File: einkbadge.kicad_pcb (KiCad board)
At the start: 2 copper layers, 7.7 x 0.9 mm, 83 parts, among them J3 USB_C_Receptacle_USB2.0_14P, J4 Conn_01x03, J6 lipo, Q1 AO3401A, Q6 Si1308EDL, SW21 SW_Push, SW22 SW_Push, SW23 SW_Push, SW3 SW_Push, SW4 SW_Push, SW5 SW_SPDT, SW7 SW_Push, U11 SRV05-4, U18 ST25DV04K-JFR6D3, U5 RP2350_60QFN, U6 NCP1117-3.3_SOT223, U9 TP4056-42-ESOP8, Y1 ABM8-272-T3

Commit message: pcb routing almost done
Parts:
- removed C100, C101, C102, C103, C104, C95, C96, C97, C98, C99: 1uF, Capacitor_SMD:C_0402_1005Metric
- removed C105, C106: 4.7uF, Capacitor_SMD:C_0603_1608Metric
- removed C107: 0.1uF, Capacitor_SMD:C_0402_1005Metric
- removed C108: 33pF, Capacitor_SMD:C_0402_1005Metric
- removed D13: LED, LED_SMD:LED_0402_1005Metric
- removed D15, D21, D22, D23: MBR0530, Diode_SMD:D_SOD-123
- removed H5, H6, H7, H8: MountingHole, MountingHole:MountingHole_2.2mm_M2_Pad_Via
- removed J3: USB_C_Receptacle_USB2.0_14P, Connector_USB:USB_C_Receptacle_GCT_USB4105-xx-A_16P_TopMnt_Horizontal
- removed J4: Conn_01x03, Connector_PinHeader_1.00mm:PinHeader_1x03_P1.00mm_Vertical
- removed J6: lipo, Connector_JST:JST_PH_B2B-PH-K_1x02_P2.00mm_Vertical
- removed L6: 47uH 500mA, Inductor_SMD:L_APV_ANR4018
- removed Q6: Si1308EDL, Package_TO_SOT_SMD:SOT-323_SC-70
- removed R29: 2.2R, Resistor_SMD:R_0402_1005Metric
- removed R30: 1M, Resistor_SMD:R_0402_1005Metric
- removed R31: 47, Resistor_SMD:R_0402_1005Metric
- removed R32, R38, R45: 10k, Resistor_SMD:R_0402_1005Metric
- removed R33: 33, Resistor_SMD:R_0402_1005Metric
- removed R34, R35, R43: 5.1k, Resistor_SMD:R_0402_1005Metric
- removed R36, R37: 27, Resistor_SMD:R_0402_1005Metric
- removed R39, R44: 1.5k, Resistor_SMD:R_0402_1005Metric
- removed R40, R42: 1k, Resistor_SMD:R_0402_1005Metric
- removed R41: 1K, Resistor_SMD:R_0402_1005Metric
- removed SW21, SW22, SW23, SW7: SW_Push, Button_Switch_THT:SW_PUSH-12mm
- removed U11: SRV05-4, Package_TO_SOT_SMD:SOT-23-6
- removed U18: ST25DV04K-JFR6D3, Package_DFN_QFN:ST_UFDFPN-12-1EP_3x3mm_P0.5mm_EP1.4x2.55mm
- removed U6: NCP1117-3.3_SOT223, Package_TO_SOT_SMD:SOT-223-3_TabPin2
- removed U9: TP4056-42-ESOP8, Package_SO:SOIC-8-1EP_3.9x4.9mm_P1.27mm_EP2.41x3.3mm_ThermalVias
- added C18: 100n, Capacitor_SMD:C_0402_1005Metric, B.Cu at (198.1, 108.6)
- added C21: 4.7uF, Capacitor_SMD:C_0603_1608Metric, B.Cu at (169.2, 105.6)
- added C24: 1uF, Capacitor_SMD:C_0402_1005Metric, B.Cu at (162.3, 95.3)
- added C25: 1uF, Capacitor_SMD:C_0402_1005Metric, B.Cu at (162.3, 100.5)
- added C26: 1uF, Capacitor_SMD:C_0402_1005Metric, B.Cu at (162.3, 101.4)
- added C27: 1uF, Capacitor_SMD:C_0402_1005Metric, B.Cu at (162.3, 103.4)
- added C28: 1uF, Capacitor_SMD:C_0402_1005Metric, B.Cu at (162.3, 105.7)
- added C29: 1uF, Capacitor_SMD:C_0402_1005Metric, B.Cu at (162.3, 108.2)
- added C30: 1uF, Capacitor_SMD:C_0402_1005Metric, B.Cu at (162.3, 96.3)
- added C31: 1uF, Capacitor_SMD:C_0402_1005Metric, B.Cu at (162.3, 102.4)
- added C32: 1uF, Capacitor_SMD:C_0402_1005Metric, B.Cu at (162.3, 104.4)
- added C33: 1uF, Capacitor_SMD:C_0402_1005Metric, B.Cu at (162.3, 106.9)
- added D1: MBR0530, Diode_SMD:D_SOD-123, B.Cu at (165.9, 109.1)
- added D2: MBR0530, Diode_SMD:D_SOD-123, B.Cu at (165.9, 106.6)
- added D3: MBR0530, Diode_SMD:D_SOD-123, B.Cu at (165.9, 104.1)
- added D4: LED, LED_SMD:LED_0805_2012Metric, B.Cu at (232.4, 83.3)
- added H1: MountingHole, MountingHole:MountingHole_2.2mm_M2_Pad_Via, F.Cu at (156.1, 124.2)
- added H2: MountingHole, MountingHole:MountingHole_2.2mm_M2_Pad_Via, F.Cu at (252.6, 124.2)
- added H3: MountingHole, MountingHole:MountingHole_2.2mm_M2_Pad_Via, F.Cu at (156.1, 157.4)
- added H4: MountingHole, MountingHole:MountingHole_2.2mm_M2_Pad_Via, F.Cu at (252.6, 157.3)
- added J1: USB_C_Receptacle_USB2.0_14P, Connector_USB:USB_C_Receptacle_GCT_USB4105-xx-A_16P_TopMnt_Horizontal, B.Cu at (243.1, 159.4)
- added J2: Conn_01x03, Connector_PinHeader_2.54mm:PinHeader_1x03_P2.54mm_Vertical, B.Cu at (152.9, 117.0)
- added L2: 47uH 500mA, Inductor_SMD:L_APV_ANR4018, B.Cu at (166.5, 99.9)
- added L3: NFC antenna, ant:KiCadAntenna, F.Cu at (254.6, 82.0)
- added R1: 5.1k, Resistor_SMD:R_0402_1005Metric, B.Cu at (245.2, 153.5)
- added R10: 1M, Resistor_SMD:R_0402_1005Metric, B.Cu at (166.3, 92.9)
- added R11: 10k, Resistor_SMD:R_0402_1005Metric, B.Cu at (236.4, 93.9)
- added R12: 2.2R, Resistor_SMD:R_0402_1005Metric, B.Cu at (166.3, 94.0)
- added R13: 47, Resistor_SMD:R_0402_1005Metric, B.Cu at (234.8, 83.3)
- added R14: 10k, Resistor_SMD:R_0402_1005Metric, B.Cu at (232.9, 92.8)
- added R2: 5.1k, Resistor_SMD:R_0402_1005Metric, B.Cu at (240.6, 153.5)
- added R3: 33, Resistor_SMD:R_0402_1005Metric, B.Cu at (209.4, 103.1)
- added R4: 1k, Resistor_SMD:R_0402_1005Metric, B.Cu at (223.1, 112.4)
- added R5: 1k, Resistor_SMD:R_0402_1005Metric, B.Cu at (223.1, 102.0)
- added R6: 1K, Resistor_SMD:R_0402_1005Metric, B.Cu at (191.3, 91.9)
- added R7: 27, Resistor_SMD:R_0402_1005Metric, B.Cu at (204.1, 108.0)
- added R8: 27, Resistor_SMD:R_0402_1005Metric, B.Cu at (204.9, 107.2)
- added R9: 10k, Resistor_SMD:R_0402_1005Metric, B.Cu at (235.4, 93.9)
- added REF**10: TestPoint_THTPad_D2.0mm_Drill1.0mm, TestPoint:TestPoint_THTPad_D2.0mm_Drill1.0mm, F.Cu at (175.1, 122.9)
- added REF**100: TestPoint_THTPad_D2.0mm_Drill1.0mm, TestPoint:TestPoint_THTPad_D2.0mm_Drill1.0mm, F.Cu at (200.5, 128.0)
- added REF**101: TestPoint_THTPad_D2.0mm_Drill1.0mm, TestPoint:TestPoint_THTPad_D2.0mm_Drill1.0mm, F.Cu at (203.1, 128.0)
- added REF**102: TestPoint_THTPad_D2.0mm_Drill1.0mm, TestPoint:TestPoint_THTPad_D2.0mm_Drill1.0mm, F.Cu at (205.6, 128.0)
- added REF**103: TestPoint_THTPad_D2.0mm_Drill1.0mm, TestPoint:TestPoint_THTPad_D2.0mm_Drill1.0mm, F.Cu at (208.1, 128.0)
- added REF**104: TestPoint_THTPad_D2.0mm_Drill1.0mm, TestPoint:TestPoint_THTPad_D2.0mm_Drill1.0mm, F.Cu at (210.7, 128.0)
- added REF**105: TestPoint_THTPad_D2.0mm_Drill1.0mm, TestPoint:TestPoint_THTPad_D2.0mm_Drill1.0mm, F.Cu at (213.2, 128.0)
- added REF**106: TestPoint_THTPad_D2.0mm_Drill1.0mm, TestPoint:TestPoint_THTPad_D2.0mm_Drill1.0mm, F.Cu at (215.8, 128.0)
- added REF**107: TestPoint_THTPad_D2.0mm_Drill1.0mm, TestPoint:TestPoint_THTPad_D2.0mm_Drill1.0mm, F.Cu at (218.3, 128.0)
- added REF**108: TestPoint_THTPad_D2.0mm_Drill1.0mm, TestPoint:TestPoint_THTPad_D2.0mm_Drill1.0mm, F.Cu at (220.8, 128.0)
- added REF**109: TestPoint_THTPad_D2.0mm_Drill1.0mm, TestPoint:TestPoint_THTPad_D2.0mm_Drill1.0mm, F.Cu at (223.4, 128.0)
- added REF**11: TestPoint_THTPad_D2.0mm_Drill1.0mm, TestPoint:TestPoint_THTPad_D2.0mm_Drill1.0mm, F.Cu at (177.7, 122.9)
- added REF**110: TestPoint_THTPad_D2.0mm_Drill1.0mm, TestPoint:TestPoint_THTPad_D2.0mm_Drill1.0mm, F.Cu at (225.9, 128.0)
- added REF**111: TestPoint_THTPad_D2.0mm_Drill1.0mm, TestPoint:TestPoint_THTPad_D2.0mm_Drill1.0mm, F.Cu at (228.5, 128.0)
- added REF**112: TestPoint_THTPad_D2.0mm_Drill1.0mm, TestPoint:TestPoint_THTPad_D2.0mm_Drill1.0mm, F.Cu at (231.0, 128.0)
- added REF**113: TestPoint_THTPad_D2.0mm_Drill1.0mm, TestPoint:TestPoint_THTPad_D2.0mm_Drill1.0mm, F.Cu at (233.5, 128.0)
- added REF**12: TestPoint_THTPad_D2.0mm_Drill1.0mm, TestPoint:TestPoint_THTPad_D2.0mm_Drill1.0mm, F.Cu at (180.2, 122.9)
- added REF**122: TestPoint_THTPad_D2.0mm_Drill1.0mm, TestPoint:TestPoint_THTPad_D2.0mm_Drill1.0mm, F.Cu at (154.8, 130.6)
- added REF**123: TestPoint_THTPad_D2.0mm_Drill1.0mm, TestPoint:TestPoint_THTPad_D2.0mm_Drill1.0mm, F.Cu at (157.3, 130.6)
- added REF**124: TestPoint_THTPad_D2.0mm_Drill1.0mm, TestPoint:TestPoint_THTPad_D2.0mm_Drill1.0mm, F.Cu at (159.9, 130.6)
- added REF**125: TestPoint_THTPad_D2.0mm_Drill1.0mm, TestPoint:TestPoint_THTPad_D2.0mm_Drill1.0mm, F.Cu at (162.4, 130.6)
- added REF**126: TestPoint_THTPad_D2.0mm_Drill1.0mm, TestPoint:TestPoint_THTPad_D2.0mm_Drill1.0mm, F.Cu at (165.0, 130.6)
- added REF**127: TestPoint_THTPad_D2.0mm_Drill1.0mm, TestPoint:TestPoint_THTPad_D2.0mm_Drill1.0mm, F.Cu at (167.5, 130.6)
- added REF**128: TestPoint_THTPad_D2.0mm_Drill1.0mm, TestPoint:TestPoint_THTPad_D2.0mm_Drill1.0mm, F.Cu at (170.0, 130.6)
- added REF**13: TestPoint_THTPad_D2.0mm_Drill1.0mm, TestPoint:TestPoint_THTPad_D2.0mm_Drill1.0mm, F.Cu at (182.7, 122.9)
- added REF**135: TestPoint_THTPad_D2.0mm_Drill1.0mm, TestPoint:TestPoint_THTPad_D2.0mm_Drill1.0mm, F.Cu at (187.8, 130.6)
- added REF**136: TestPoint_THTPad_D2.0mm_Drill1.0mm, TestPoint:TestPoint_THTPad_D2.0mm_Drill1.0mm, F.Cu at (190.4, 130.6)
- added REF**137: TestPoint_THTPad_D2.0mm_Drill1.0mm, TestPoint:TestPoint_THTPad_D2.0mm_Drill1.0mm, F.Cu at (192.9, 130.6)
- added REF**138: TestPoint_THTPad_D2.0mm_Drill1.0mm, TestPoint:TestPoint_THTPad_D2.0mm_Drill1.0mm, F.Cu at (195.4, 130.6)
- added REF**139: TestPoint_THTPad_D2.0mm_Drill1.0mm, TestPoint:TestPoint_THTPad_D2.0mm_Drill1.0mm, F.Cu at (198.0, 130.6)
- added REF**14: TestPoint_THTPad_D2.0mm_Drill1.0mm, TestPoint:TestPoint_THTPad_D2.0mm_Drill1.0mm, F.Cu at (185.3, 122.9)
- added REF**140: TestPoint_THTPad_D2.0mm_Drill1.0mm, TestPoint:TestPoint_THTPad_D2.0mm_Drill1.0mm, F.Cu at (200.5, 130.6)
- added REF**141: TestPoint_THTPad_D2.0mm_Drill1.0mm, TestPoint:TestPoint_THTPad_D2.0mm_Drill1.0mm, F.Cu at (203.1, 130.6)
- added REF**142: TestPoint_THTPad_D2.0mm_Drill1.0mm, TestPoint:TestPoint_THTPad_D2.0mm_Drill1.0mm, F.Cu at (205.6, 130.6)
- added REF**143: TestPoint_THTPad_D2.0mm_Drill1.0mm, TestPoint:TestPoint_THTPad_D2.0mm_Drill1.0mm, F.Cu at (208.1, 130.6)
- added REF**144: TestPoint_THTPad_D2.0mm_Drill1.0mm, TestPoint:TestPoint_THTPad_D2.0mm_Drill1.0mm, F.Cu at (210.7, 130.6)
- added REF**145: TestPoint_THTPad_D2.0mm_Drill1.0mm, TestPoint:TestPoint_THTPad_D2.0mm_Drill1.0mm, F.Cu at (213.2, 130.6)
- added REF**146: TestPoint_THTPad_D2.0mm_Drill1.0mm, TestPoint:TestPoint_THTPad_D2.0mm_Drill1.0mm, F.Cu at (215.8, 130.6)
- added REF**147: TestPoint_THTPad_D2.0mm_Drill1.0mm, TestPoint:TestPoint_THTPad_D2.0mm_Drill1.0mm, F.Cu at (218.3, 130.6)
- added REF**148: TestPoint_THTPad_D2.0mm_Drill1.0mm, TestPoint:TestPoint_THTPad_D2.0mm_Drill1.0mm, F.Cu at (220.8, 130.6)
- added REF**149: TestPoint_THTPad_D2.0mm_Drill1.0mm, TestPoint:TestPoint_THTPad_D2.0mm_Drill1.0mm, F.Cu at (223.4, 130.6)
- added REF**15: TestPoint_THTPad_D2.0mm_Drill1.0mm, TestPoint:TestPoint_THTPad_D2.0mm_Drill1.0mm, F.Cu at (187.8, 122.9)
- added REF**150: TestPoint_THTPad_D2.0mm_Drill1.0mm, TestPoint:TestPoint_THTPad_D2.0mm_Drill1.0mm, F.Cu at (225.9, 130.6)
- added REF**151: TestPoint_THTPad_D2.0mm_Drill1.0mm, TestPoint:TestPoint_THTPad_D2.0mm_Drill1.0mm, F.Cu at (228.5, 130.6)
- added REF**152: TestPoint_THTPad_D2.0mm_Drill1.0mm, TestPoint:TestPoint_THTPad_D2.0mm_Drill1.0mm, F.Cu at (231.0, 130.6)
- added REF**153: TestPoint_THTPad_D2.0mm_Drill1.0mm, TestPoint:TestPoint_THTPad_D2.0mm_Drill1.0mm, F.Cu at (233.5, 130.6)
- added REF**16: TestPoint_THTPad_D2.0mm_Drill1.0mm, TestPoint:TestPoint_THTPad_D2.0mm_Drill1.0mm, F.Cu at (190.4, 122.9)
- added REF**162: TestPoint_THTPad_D2.0mm_Drill1.0mm, TestPoint:TestPoint_THTPad_D2.0mm_Drill1.0mm, F.Cu at (154.8, 133.1)
- added REF**163: TestPoint_THTPad_D2.0mm_Drill1.0mm, TestPoint:TestPoint_THTPad_D2.0mm_Drill1.0mm, F.Cu at (157.3, 133.1)
- added REF**164: TestPoint_THTPad_D2.0mm_Drill1.0mm, TestPoint:TestPoint_THTPad_D2.0mm_Drill1.0mm, F.Cu at (159.9, 133.1)
- added REF**165: TestPoint_THTPad_D2.0mm_Drill1.0mm, TestPoint:TestPoint_THTPad_D2.0mm_Drill1.0mm, F.Cu at (162.4, 133.1)
- added REF**166: TestPoint_THTPad_D2.0mm_Drill1.0mm, TestPoint:TestPoint_THTPad_D2.0mm_Drill1.0mm, F.Cu at (165.0, 133.1)
- added REF**167: TestPoint_THTPad_D2.0mm_Drill1.0mm, TestPoint:TestPoint_THTPad_D2.0mm_Drill1.0mm, F.Cu at (167.5, 133.1)
- added REF**168: TestPoint_THTPad_D2.0mm_Drill1.0mm, TestPoint:TestPoint_THTPad_D2.0mm_Drill1.0mm, F.Cu at (170.0, 133.1)
- added REF**169: TestPoint_THTPad_D2.0mm_Drill1.0mm, TestPoint:TestPoint_THTPad_D2.0mm_Drill1.0mm, F.Cu at (172.6, 133.1)
- added REF**17: TestPoint_THTPad_D2.0mm_Drill1.0mm, TestPoint:TestPoint_THTPad_D2.0mm_Drill1.0mm, F.Cu at (192.9, 122.9)
- added REF**170: TestPoint_THTPad_D2.0mm_Drill1.0mm, TestPoint:TestPoint_THTPad_D2.0mm_Drill1.0mm, F.Cu at (175.1, 133.1)
- added REF**171: TestPoint_THTPad_D2.0mm_Drill1.0mm, TestPoint:TestPoint_THTPad_D2.0mm_Drill1.0mm, F.Cu at (177.7, 133.1)
- added REF**172: TestPoint_THTPad_D2.0mm_Drill1.0mm, TestPoint:TestPoint_THTPad_D2.0mm_Drill1.0mm, F.Cu at (180.2, 133.1)
- added REF**173: TestPoint_THTPad_D2.0mm_Drill1.0mm, TestPoint:TestPoint_THTPad_D2.0mm_Drill1.0mm, F.Cu at (182.7, 133.1)
- added REF**174: TestPoint_THTPad_D2.0mm_Drill1.0mm, TestPoint:TestPoint_THTPad_D2.0mm_Drill1.0mm, F.Cu at (185.3, 133.1)
- added REF**175: TestPoint_THTPad_D2.0mm_Drill1.0mm, TestPoint:TestPoint_THTPad_D2.0mm_Drill1.0mm, F.Cu at (187.8, 133.1)
- added REF**176: TestPoint_THTPad_D2.0mm_Drill1.0mm, TestPoint:TestPoint_THTPad_D2.0mm_Drill1.0mm, F.Cu at (190.4, 133.1)
- added REF**177: TestPoint_THTPad_D2.0mm_Drill1.0mm, TestPoint:TestPoint_THTPad_D2.0mm_Drill1.0mm, F.Cu at (192.9, 133.1)
- added REF**178: TestPoint_THTPad_D2.0mm_Drill1.0mm, TestPoint:TestPoint_THTPad_D2.0mm_Drill1.0mm, F.Cu at (195.4, 133.1)
- added REF**179: TestPoint_THTPad_D2.0mm_Drill1.0mm, TestPoint:TestPoint_THTPad_D2.0mm_Drill1.0mm, F.Cu at (198.0, 133.1)
- added REF**18: TestPoint_THTPad_D2.0mm_Drill1.0mm, TestPoint:TestPoint_THTPad_D2.0mm_Drill1.0mm, F.Cu at (195.4, 122.9)
- added REF**180: TestPoint_THTPad_D2.0mm_Drill1.0mm, TestPoint:TestPoint_THTPad_D2.0mm_Drill1.0mm, F.Cu at (200.5, 133.1)
- added REF**181: TestPoint_THTPad_D2.0mm_Drill1.0mm, TestPoint:TestPoint_THTPad_D2.0mm_Drill1.0mm, F.Cu at (203.1, 133.1)
- added REF**182: TestPoint_THTPad_D2.0mm_Drill1.0mm, TestPoint:TestPoint_THTPad_D2.0mm_Drill1.0mm, F.Cu at (205.6, 133.1)
- added REF**183: TestPoint_THTPad_D2.0mm_Drill1.0mm, TestPoint:TestPoint_THTPad_D2.0mm_Drill1.0mm, F.Cu at (208.1, 133.1)
- added REF**184: TestPoint_THTPad_D2.0mm_Drill1.0mm, TestPoint:TestPoint_THTPad_D2.0mm_Drill1.0mm, F.Cu at (210.7, 133.1)
- added REF**185: TestPoint_THTPad_D2.0mm_Drill1.0mm, TestPoint:TestPoint_THTPad_D2.0mm_Drill1.0mm, F.Cu at (213.2, 133.1)
- added REF**186: TestPoint_THTPad_D2.0mm_Drill1.0mm, TestPoint:TestPoint_THTPad_D2.0mm_Drill1.0mm, F.Cu at (215.8, 133.1)
- added REF**187: TestPoint_THTPad_D2.0mm_Drill1.0mm, TestPoint:TestPoint_THTPad_D2.0mm_Drill1.0mm, F.Cu at (218.3, 133.1)
- added REF**188: TestPoint_THTPad_D2.0mm_Drill1.0mm, TestPoint:TestPoint_THTPad_D2.0mm_Drill1.0mm, F.Cu at (220.8, 133.1)
- added REF**189: TestPoint_THTPad_D2.0mm_Drill1.0mm, TestPoint:TestPoint_THTPad_D2.0mm_Drill1.0mm, F.Cu at (223.4, 133.1)
- added REF**19: TestPoint_THTPad_D2.0mm_Drill1.0mm, TestPoint:TestPoint_THTPad_D2.0mm_Drill1.0mm, F.Cu at (198.0, 122.9)
- added REF**190: TestPoint_THTPad_D2.0mm_Drill1.0mm, TestPoint:TestPoint_THTPad_D2.0mm_Drill1.0mm, F.Cu at (225.9, 133.1)
- added REF**191: TestPoint_THTPad_D2.0mm_Drill1.0mm, TestPoint:TestPoint_THTPad_D2.0mm_Drill1.0mm, F.Cu at (228.5, 133.1)
- added REF**192: TestPoint_THTPad_D2.0mm_Drill1.0mm, TestPoint:TestPoint_THTPad_D2.0mm_Drill1.0mm, F.Cu at (231.0, 133.1)
- added REF**193: TestPoint_THTPad_D2.0mm_Drill1.0mm, TestPoint:TestPoint_THTPad_D2.0mm_Drill1.0mm, F.Cu at (233.5, 133.1)
- added REF**194: TestPoint_THTPad_D2.0mm_Drill1.0mm, TestPoint:TestPoint_THTPad_D2.0mm_Drill1.0mm, F.Cu at (236.1, 133.1)
- added REF**20: TestPoint_THTPad_D2.0mm_Drill1.0mm, TestPoint:TestPoint_THTPad_D2.0mm_Drill1.0mm, F.Cu at (200.5, 122.9)
- added REF**202: TestPoint_THTPad_D2.0mm_Drill1.0mm, TestPoint:TestPoint_THTPad_D2.0mm_Drill1.0mm, F.Cu at (154.8, 135.6)
- added REF**203: TestPoint_THTPad_D2.0mm_Drill1.0mm, TestPoint:TestPoint_THTPad_D2.0mm_Drill1.0mm, F.Cu at (157.3, 135.6)
- added REF**204: TestPoint_THTPad_D2.0mm_Drill1.0mm, TestPoint:TestPoint_THTPad_D2.0mm_Drill1.0mm, F.Cu at (159.9, 135.6)
- added REF**205: TestPoint_THTPad_D2.0mm_Drill1.0mm, TestPoint:TestPoint_THTPad_D2.0mm_Drill1.0mm, F.Cu at (162.4, 135.6)
- added REF**206: TestPoint_THTPad_D2.0mm_Drill1.0mm, TestPoint:TestPoint_THTPad_D2.0mm_Drill1.0mm, F.Cu at (165.0, 135.6)
- added REF**207: TestPoint_THTPad_D2.0mm_Drill1.0mm, TestPoint:TestPoint_THTPad_D2.0mm_Drill1.0mm, F.Cu at (167.5, 135.6)
- added REF**208: TestPoint_THTPad_D2.0mm_Drill1.0mm, TestPoint:TestPoint_THTPad_D2.0mm_Drill1.0mm, F.Cu at (170.0, 135.6)
- added REF**209: TestPoint_THTPad_D2.0mm_Drill1.0mm, TestPoint:TestPoint_THTPad_D2.0mm_Drill1.0mm, F.Cu at (172.6, 135.6)
- added REF**21: TestPoint_THTPad_D2.0mm_Drill1.0mm, TestPoint:TestPoint_THTPad_D2.0mm_Drill1.0mm, F.Cu at (203.1, 122.9)
- added REF**210: TestPoint_THTPad_D2.0mm_Drill1.0mm, TestPoint:TestPoint_THTPad_D2.0mm_Drill1.0mm, F.Cu at (175.1, 135.6)
- added REF**211: TestPoint_THTPad_D2.0mm_Drill1.0mm, TestPoint:TestPoint_THTPad_D2.0mm_Drill1.0mm, F.Cu at (177.7, 135.6)
- added REF**212: TestPoint_THTPad_D2.0mm_Drill1.0mm, TestPoint:TestPoint_THTPad_D2.0mm_Drill1.0mm, F.Cu at (180.2, 135.6)
- added REF**213: TestPoint_THTPad_D2.0mm_Drill1.0mm, TestPoint:TestPoint_THTPad_D2.0mm_Drill1.0mm, F.Cu at (182.7, 135.6)
- added REF**214: TestPoint_THTPad_D2.0mm_Drill1.0mm, TestPoint:TestPoint_THTPad_D2.0mm_Drill1.0mm, F.Cu at (185.3, 135.6)
- added REF**215: TestPoint_THTPad_D2.0mm_Drill1.0mm, TestPoint:TestPoint_THTPad_D2.0mm_Drill1.0mm, F.Cu at (187.8, 135.6)
- added REF**216: TestPoint_THTPad_D2.0mm_Drill1.0mm, TestPoint:TestPoint_THTPad_D2.0mm_Drill1.0mm, F.Cu at (190.4, 135.6)
- added REF**217: TestPoint_THTPad_D2.0mm_Drill1.0mm, TestPoint:TestPoint_THTPad_D2.0mm_Drill1.0mm, F.Cu at (192.9, 135.6)
- added REF**218: TestPoint_THTPad_D2.0mm_Drill1.0mm, TestPoint:TestPoint_THTPad_D2.0mm_Drill1.0mm, F.Cu at (195.4, 135.6)
- added REF**219: TestPoint_THTPad_D2.0mm_Drill1.0mm, TestPoint:TestPoint_THTPad_D2.0mm_Drill1.0mm, F.Cu at (198.0, 135.6)
- added REF**22: TestPoint_THTPad_D2.0mm_Drill1.0mm, TestPoint:TestPoint_THTPad_D2.0mm_Drill1.0mm, F.Cu at (205.6, 122.9)
- added REF**220: TestPoint_THTPad_D2.0mm_Drill1.0mm, TestPoint:TestPoint_THTPad_D2.0mm_Drill1.0mm, F.Cu at (200.5, 135.6)
- added REF**221: TestPoint_THTPad_D2.0mm_Drill1.0mm, TestPoint:TestPoint_THTPad_D2.0mm_Drill1.0mm, F.Cu at (203.1, 135.6)
- added REF**222: TestPoint_THTPad_D2.0mm_Drill1.0mm, TestPoint:TestPoint_THTPad_D2.0mm_Drill1.0mm, F.Cu at (205.6, 135.6)
- added REF**223: TestPoint_THTPad_D2.0mm_Drill1.0mm, TestPoint:TestPoint_THTPad_D2.0mm_Drill1.0mm, F.Cu at (208.1, 135.6)
- added REF**224: TestPoint_THTPad_D2.0mm_Drill1.0mm, TestPoint:TestPoint_THTPad_D2.0mm_Drill1.0mm, F.Cu at (210.7, 135.6)
- added REF**225: TestPoint_THTPad_D2.0mm_Drill1.0mm, TestPoint:TestPoint_THTPad_D2.0mm_Drill1.0mm, F.Cu at (213.2, 135.6)
- added REF**226: TestPoint_THTPad_D2.0mm_Drill1.0mm, TestPoint:TestPoint_THTPad_D2.0mm_Drill1.0mm, F.Cu at (215.8, 135.6)
- added REF**227: TestPoint_THTPad_D2.0mm_Drill1.0mm, TestPoint:TestPoint_THTPad_D2.0mm_Drill1.0mm, F.Cu at (218.3, 135.6)
- added REF**228: TestPoint_THTPad_D2.0mm_Drill1.0mm, TestPoint:TestPoint_THTPad_D2.0mm_Drill1.0mm, F.Cu at (220.8, 135.6)
- added REF**229: TestPoint_THTPad_D2.0mm_Drill1.0mm, TestPoint:TestPoint_THTPad_D2.0mm_Drill1.0mm, F.Cu at (223.4, 135.6)
- added REF**23: TestPoint_THTPad_D2.0mm_Drill1.0mm, TestPoint:TestPoint_THTPad_D2.0mm_Drill1.0mm, F.Cu at (208.1, 122.9)
- added REF**230: TestPoint_THTPad_D2.0mm_Drill1.0mm, TestPoint:TestPoint_THTPad_D2.0mm_Drill1.0mm, F.Cu at (225.9, 135.6)
- added REF**231: TestPoint_THTPad_D2.0mm_Drill1.0mm, TestPoint:TestPoint_THTPad_D2.0mm_Drill1.0mm, F.Cu at (228.5, 135.6)
- added REF**232: TestPoint_THTPad_D2.0mm_Drill1.0mm, TestPoint:TestPoint_THTPad_D2.0mm_Drill1.0mm, F.Cu at (231.0, 135.6)
- added REF**233: TestPoint_THTPad_D2.0mm_Drill1.0mm, TestPoint:TestPoint_THTPad_D2.0mm_Drill1.0mm, F.Cu at (233.5, 135.6)
- added REF**24: TestPoint_THTPad_D2.0mm_Drill1.0mm, TestPoint:TestPoint_THTPad_D2.0mm_Drill1.0mm, F.Cu at (210.7, 122.9)
- added REF**242: TestPoint_THTPad_D2.0mm_Drill1.0mm, TestPoint:TestPoint_THTPad_D2.0mm_Drill1.0mm, F.Cu at (154.8, 138.2)
- added REF**243: TestPoint_THTPad_D2.0mm_Drill1.0mm, TestPoint:TestPoint_THTPad_D2.0mm_Drill1.0mm, F.Cu at (157.3, 138.2)
- added REF**25: TestPoint_THTPad_D2.0mm_Drill1.0mm, TestPoint:TestPoint_THTPad_D2.0mm_Drill1.0mm, F.Cu at (213.2, 122.9)
- added REF**250: TestPoint_THTPad_D2.0mm_Drill1.0mm, TestPoint:TestPoint_THTPad_D2.0mm_Drill1.0mm, F.Cu at (175.1, 138.2)
- added REF**251: TestPoint_THTPad_D2.0mm_Drill1.0mm, TestPoint:TestPoint_THTPad_D2.0mm_Drill1.0mm, F.Cu at (177.7, 138.2)
- added REF**252: TestPoint_THTPad_D2.0mm_Drill1.0mm, TestPoint:TestPoint_THTPad_D2.0mm_Drill1.0mm, F.Cu at (180.2, 138.2)
- added REF**253: TestPoint_THTPad_D2.0mm_Drill1.0mm, TestPoint:TestPoint_THTPad_D2.0mm_Drill1.0mm, F.Cu at (182.7, 138.2)
- added REF**26: TestPoint_THTPad_D2.0mm_Drill1.0mm, TestPoint:TestPoint_THTPad_D2.0mm_Drill1.0mm, F.Cu at (215.8, 122.9)
- added REF**260: TestPoint_THTPad_D2.0mm_Drill1.0mm, TestPoint:TestPoint_THTPad_D2.0mm_Drill1.0mm, F.Cu at (200.5, 138.2)
- added REF**261: TestPoint_THTPad_D2.0mm_Drill1.0mm, TestPoint:TestPoint_THTPad_D2.0mm_Drill1.0mm, F.Cu at (203.1, 138.2)
- added REF**262: TestPoint_THTPad_D2.0mm_Drill1.0mm, TestPoint:TestPoint_THTPad_D2.0mm_Drill1.0mm, F.Cu at (205.6, 138.2)
- added REF**263: TestPoint_THTPad_D2.0mm_Drill1.0mm, TestPoint:TestPoint_THTPad_D2.0mm_Drill1.0mm, F.Cu at (208.1, 138.2)
- added REF**264: TestPoint_THTPad_D2.0mm_Drill1.0mm, TestPoint:TestPoint_THTPad_D2.0mm_Drill1.0mm, F.Cu at (210.7, 138.2)
- added REF**265: TestPoint_THTPad_D2.0mm_Drill1.0mm, TestPoint:TestPoint_THTPad_D2.0mm_Drill1.0mm, F.Cu at (213.2, 138.2)
- added REF**266: TestPoint_THTPad_D2.0mm_Drill1.0mm, TestPoint:TestPoint_THTPad_D2.0mm_Drill1.0mm, F.Cu at (215.8, 138.2)
- added REF**267: TestPoint_THTPad_D2.0mm_Drill1.0mm, TestPoint:TestPoint_THTPad_D2.0mm_Drill1.0mm, F.Cu at (218.3, 138.2)
- added REF**268: TestPoint_THTPad_D2.0mm_Drill1.0mm, TestPoint:TestPoint_THTPad_D2.0mm_Drill1.0mm, F.Cu at (220.8, 138.2)
- added REF**269: TestPoint_THTPad_D2.0mm_Drill1.0mm, TestPoint:TestPoint_THTPad_D2.0mm_Drill1.0mm, F.Cu at (223.4, 138.2)
- added REF**27: TestPoint_THTPad_D2.0mm_Drill1.0mm, TestPoint:TestPoint_THTPad_D2.0mm_Drill1.0mm, F.Cu at (218.3, 122.9)
- added REF**270: TestPoint_THTPad_D2.0mm_Drill1.0mm, TestPoint:TestPoint_THTPad_D2.0mm_Drill1.0mm, F.Cu at (225.9, 138.2)
- added REF**271: TestPoint_THTPad_D2.0mm_Drill1.0mm, TestPoint:TestPoint_THTPad_D2.0mm_Drill1.0mm, F.Cu at (228.5, 138.2)
- added REF**272: TestPoint_THTPad_D2.0mm_Drill1.0mm, TestPoint:TestPoint_THTPad_D2.0mm_Drill1.0mm, F.Cu at (231.0, 138.2)
- added REF**273: TestPoint_THTPad_D2.0mm_Drill1.0mm, TestPoint:TestPoint_THTPad_D2.0mm_Drill1.0mm, F.Cu at (233.5, 138.2)
- added REF**274: TestPoint_THTPad_D2.0mm_Drill1.0mm, TestPoint:TestPoint_THTPad_D2.0mm_Drill1.0mm, F.Cu at (236.1, 138.2)
- added REF**28: TestPoint_THTPad_D2.0mm_Drill1.0mm, TestPoint:TestPoint_THTPad_D2.0mm_Drill1.0mm, F.Cu at (220.8, 122.9)
- added REF**282: TestPoint_THTPad_D2.0mm_Drill1.0mm, TestPoint:TestPoint_THTPad_D2.0mm_Drill1.0mm, F.Cu at (154.8, 140.7)
- added REF**283: TestPoint_THTPad_D2.0mm_Drill1.0mm, TestPoint:TestPoint_THTPad_D2.0mm_Drill1.0mm, F.Cu at (157.3, 140.7)
- added REF**284: TestPoint_THTPad_D2.0mm_Drill1.0mm, TestPoint:TestPoint_THTPad_D2.0mm_Drill1.0mm, F.Cu at (159.9, 140.7)
- added REF**289: TestPoint_THTPad_D2.0mm_Drill1.0mm, TestPoint:TestPoint_THTPad_D2.0mm_Drill1.0mm, F.Cu at (172.6, 140.7)
- added REF**29: TestPoint_THTPad_D2.0mm_Drill1.0mm, TestPoint:TestPoint_THTPad_D2.0mm_Drill1.0mm, F.Cu at (223.4, 122.9)
- added REF**290: TestPoint_THTPad_D2.0mm_Drill1.0mm, TestPoint:TestPoint_THTPad_D2.0mm_Drill1.0mm, F.Cu at (175.1, 140.7)
- added REF**291: TestPoint_THTPad_D2.0mm_Drill1.0mm, TestPoint:TestPoint_THTPad_D2.0mm_Drill1.0mm, F.Cu at (177.7, 140.7)
- added REF**292: TestPoint_THTPad_D2.0mm_Drill1.0mm, TestPoint:TestPoint_THTPad_D2.0mm_Drill1.0mm, F.Cu at (180.2, 140.7)
- added REF**293: TestPoint_THTPad_D2.0mm_Drill1.0mm, TestPoint:TestPoint_THTPad_D2.0mm_Drill1.0mm, F.Cu at (182.7, 140.7)
- added REF**294: TestPoint_THTPad_D2.0mm_Drill1.0mm, TestPoint:TestPoint_THTPad_D2.0mm_Drill1.0mm, F.Cu at (185.3, 140.7)
- added REF**299: TestPoint_THTPad_D2.0mm_Drill1.0mm, TestPoint:TestPoint_THTPad_D2.0mm_Drill1.0mm, F.Cu at (198.0, 140.7)
- added REF**30: TestPoint_THTPad_D2.0mm_Drill1.0mm, TestPoint:TestPoint_THTPad_D2.0mm_Drill1.0mm, F.Cu at (225.9, 122.9)
- added REF**300: TestPoint_THTPad_D2.0mm_Drill1.0mm, TestPoint:TestPoint_THTPad_D2.0mm_Drill1.0mm, F.Cu at (200.5, 140.7)
- added REF**301: TestPoint_THTPad_D2.0mm_Drill1.0mm, TestPoint:TestPoint_THTPad_D2.0mm_Drill1.0mm, F.Cu at (203.1, 140.7)
- added REF**302: TestPoint_THTPad_D2.0mm_Drill1.0mm, TestPoint:TestPoint_THTPad_D2.0mm_Drill1.0mm, F.Cu at (205.6, 140.7)
- added REF**303: TestPoint_THTPad_D2.0mm_Drill1.0mm, TestPoint:TestPoint_THTPad_D2.0mm_Drill1.0mm, F.Cu at (208.1, 140.7)
- added REF**304: TestPoint_THTPad_D2.0mm_Drill1.0mm, TestPoint:TestPoint_THTPad_D2.0mm_Drill1.0mm, F.Cu at (210.7, 140.7)
- added REF**305: TestPoint_THTPad_D2.0mm_Drill1.0mm, TestPoint:TestPoint_THTPad_D2.0mm_Drill1.0mm, F.Cu at (213.2, 140.7)
- added REF**306: TestPoint_THTPad_D2.0mm_Drill1.0mm, TestPoint:TestPoint_THTPad_D2.0mm_Drill1.0mm, F.Cu at (215.8, 140.7)
- added REF**307: TestPoint_THTPad_D2.0mm_Drill1.0mm, TestPoint:TestPoint_THTPad_D2.0mm_Drill1.0mm, F.Cu at (218.3, 140.7)
- added REF**308: TestPoint_THTPad_D2.0mm_Drill1.0mm, TestPoint:TestPoint_THTPad_D2.0mm_Drill1.0mm, F.Cu at (220.8, 140.7)
- added REF**309: TestPoint_THTPad_D2.0mm_Drill1.0mm, TestPoint:TestPoint_THTPad_D2.0mm_Drill1.0mm, F.Cu at (223.4, 140.7)
- added REF**31: TestPoint_THTPad_D2.0mm_Drill1.0mm, TestPoint:TestPoint_THTPad_D2.0mm_Drill1.0mm, F.Cu at (228.5, 122.9)
- added REF**310: TestPoint_THTPad_D2.0mm_Drill1.0mm, TestPoint:TestPoint_THTPad_D2.0mm_Drill1.0mm, F.Cu at (225.9, 140.7)
- added REF**311: TestPoint_THTPad_D2.0mm_Drill1.0mm, TestPoint:TestPoint_THTPad_D2.0mm_Drill1.0mm, F.Cu at (228.5, 140.7)
- added REF**312: TestPoint_THTPad_D2.0mm_Drill1.0mm, TestPoint:TestPoint_THTPad_D2.0mm_Drill1.0mm, F.Cu at (231.0, 140.7)
- added REF**313: TestPoint_THTPad_D2.0mm_Drill1.0mm, TestPoint:TestPoint_THTPad_D2.0mm_Drill1.0mm, F.Cu at (233.5, 140.7)
- added REF**314: TestPoint_THTPad_D2.0mm_Drill1.0mm, TestPoint:TestPoint_THTPad_D2.0mm_Drill1.0mm, F.Cu at (236.1, 140.7)
- added REF**322: TestPoint_THTPad_D2.0mm_Drill1.0mm, TestPoint:TestPoint_THTPad_D2.0mm_Drill1.0mm, F.Cu at (154.8, 143.3)
- added REF**323: TestPoint_THTPad_D2.0mm_Drill1.0mm, TestPoint:TestPoint_THTPad_D2.0mm_Drill1.0mm, F.Cu at (157.3, 143.3)
- added REF**330: TestPoint_THTPad_D2.0mm_Drill1.0mm, TestPoint:TestPoint_THTPad_D2.0mm_Drill1.0mm, F.Cu at (175.1, 143.3)
- added REF**331: TestPoint_THTPad_D2.0mm_Drill1.0mm, TestPoint:TestPoint_THTPad_D2.0mm_Drill1.0mm, F.Cu at (177.7, 143.3)
- added REF**332: TestPoint_THTPad_D2.0mm_Drill1.0mm, TestPoint:TestPoint_THTPad_D2.0mm_Drill1.0mm, F.Cu at (180.2, 143.3)
- added REF**333: TestPoint_THTPad_D2.0mm_Drill1.0mm, TestPoint:TestPoint_THTPad_D2.0mm_Drill1.0mm, F.Cu at (182.7, 143.3)
- added REF**340: TestPoint_THTPad_D2.0mm_Drill1.0mm, TestPoint:TestPoint_THTPad_D2.0mm_Drill1.0mm, F.Cu at (200.5, 143.3)
- added REF**341: TestPoint_THTPad_D2.0mm_Drill1.0mm, TestPoint:TestPoint_THTPad_D2.0mm_Drill1.0mm, F.Cu at (203.1, 143.3)
- added REF**342: TestPoint_THTPad_D2.0mm_Drill1.0mm, TestPoint:TestPoint_THTPad_D2.0mm_Drill1.0mm, F.Cu at (205.6, 143.3)
- added REF**343: TestPoint_THTPad_D2.0mm_Drill1.0mm, TestPoint:TestPoint_THTPad_D2.0mm_Drill1.0mm, F.Cu at (208.1, 143.3)
- added REF**344: TestPoint_THTPad_D2.0mm_Drill1.0mm, TestPoint:TestPoint_THTPad_D2.0mm_Drill1.0mm, F.Cu at (210.7, 143.3)
- added REF**345: TestPoint_THTPad_D2.0mm_Drill1.0mm, TestPoint:TestPoint_THTPad_D2.0mm_Drill1.0mm, F.Cu at (213.2, 143.3)
- added REF**346: TestPoint_THTPad_D2.0mm_Drill1.0mm, TestPoint:TestPoint_THTPad_D2.0mm_Drill1.0mm, F.Cu at (215.8, 143.3)
- added REF**347: TestPoint_THTPad_D2.0mm_Drill1.0mm, TestPoint:TestPoint_THTPad_D2.0mm_Drill1.0mm, F.Cu at (218.3, 143.3)
- added REF**348: TestPoint_THTPad_D2.0mm_Drill1.0mm, TestPoint:TestPoint_THTPad_D2.0mm_Drill1.0mm, F.Cu at (220.8, 143.3)
- added REF**362: TestPoint_THTPad_D2.0mm_Drill1.0mm, TestPoint:TestPoint_THTPad_D2.0mm_Drill1.0mm, F.Cu at (154.8, 145.8)
- added REF**363: TestPoint_THTPad_D2.0mm_Drill1.0mm, TestPoint:TestPoint_THTPad_D2.0mm_Drill1.0mm, F.Cu at (157.3, 145.8)
- added REF**364: TestPoint_THTPad_D2.0mm_Drill1.0mm, TestPoint:TestPoint_THTPad_D2.0mm_Drill1.0mm, F.Cu at (159.9, 145.8)
- added REF**365: TestPoint_THTPad_D2.0mm_Drill1.0mm, TestPoint:TestPoint_THTPad_D2.0mm_Drill1.0mm, F.Cu at (162.4, 145.8)
- added REF**366: TestPoint_THTPad_D2.0mm_Drill1.0mm, TestPoint:TestPoint_THTPad_D2.0mm_Drill1.0mm, F.Cu at (165.0, 145.8)
- added REF**367: TestPoint_THTPad_D2.0mm_Drill1.0mm, TestPoint:TestPoint_THTPad_D2.0mm_Drill1.0mm, F.Cu at (167.5, 145.8)
- added REF**368: TestPoint_THTPad_D2.0mm_Drill1.0mm, TestPoint:TestPoint_THTPad_D2.0mm_Drill1.0mm, F.Cu at (170.0, 145.8)
- added REF**369: TestPoint_THTPad_D2.0mm_Drill1.0mm, TestPoint:TestPoint_THTPad_D2.0mm_Drill1.0mm, F.Cu at (172.6, 145.8)
- added REF**370: TestPoint_THTPad_D2.0mm_Drill1.0mm, TestPoint:TestPoint_THTPad_D2.0mm_Drill1.0mm, F.Cu at (175.1, 145.8)
- added REF**371: TestPoint_THTPad_D2.0mm_Drill1.0mm, TestPoint:TestPoint_THTPad_D2.0mm_Drill1.0mm, F.Cu at (177.7, 145.8)
- added REF**372: TestPoint_THTPad_D2.0mm_Drill1.0mm, TestPoint:TestPoint_THTPad_D2.0mm_Drill1.0mm, F.Cu at (180.2, 145.8)
- added REF**373: TestPoint_THTPad_D2.0mm_Drill1.0mm, TestPoint:TestPoint_THTPad_D2.0mm_Drill1.0mm, F.Cu at (182.7, 145.8)
- added REF**374: TestPoint_THTPad_D2.0mm_Drill1.0mm, TestPoint:TestPoint_THTPad_D2.0mm_Drill1.0mm, F.Cu at (185.3, 145.8)
- added REF**375: TestPoint_THTPad_D2.0mm_Drill1.0mm, TestPoint:TestPoint_THTPad_D2.0mm_Drill1.0mm, F.Cu at (187.8, 145.8)
- added REF**376: TestPoint_THTPad_D2.0mm_Drill1.0mm, TestPoint:TestPoint_THTPad_D2.0mm_Drill1.0mm, F.Cu at (190.4, 145.8)
- added REF**377: TestPoint_THTPad_D2.0mm_Drill1.0mm, TestPoint:TestPoint_THTPad_D2.0mm_Drill1.0mm, F.Cu at (192.9, 145.8)
- added REF**378: TestPoint_THTPad_D2.0mm_Drill1.0mm, TestPoint:TestPoint_THTPad_D2.0mm_Drill1.0mm, F.Cu at (195.4, 145.8)
- added REF**379: TestPoint_THTPad_D2.0mm_Drill1.0mm, TestPoint:TestPoint_THTPad_D2.0mm_Drill1.0mm, F.Cu at (198.0, 145.8)
- added REF**380: TestPoint_THTPad_D2.0mm_Drill1.0mm, TestPoint:TestPoint_THTPad_D2.0mm_Drill1.0mm, F.Cu at (200.5, 145.8)
- added REF**381: TestPoint_THTPad_D2.0mm_Drill1.0mm, TestPoint:TestPoint_THTPad_D2.0mm_Drill1.0mm, F.Cu at (203.1, 145.8)
- added REF**382: TestPoint_THTPad_D2.0mm_Drill1.0mm, TestPoint:TestPoint_THTPad_D2.0mm_Drill1.0mm, F.Cu at (205.6, 145.8)
- added REF**383: TestPoint_THTPad_D2.0mm_Drill1.0mm, TestPoint:TestPoint_THTPad_D2.0mm_Drill1.0mm, F.Cu at (208.1, 145.8)
- added REF**384: TestPoint_THTPad_D2.0mm_Drill1.0mm, TestPoint:TestPoint_THTPad_D2.0mm_Drill1.0mm, F.Cu at (210.7, 145.8)
- added REF**385: TestPoint_THTPad_D2.0mm_Drill1.0mm, TestPoint:TestPoint_THTPad_D2.0mm_Drill1.0mm, F.Cu at (213.2, 145.8)
- added REF**386: TestPoint_THTPad_D2.0mm_Drill1.0mm, TestPoint:TestPoint_THTPad_D2.0mm_Drill1.0mm, F.Cu at (215.8, 145.8)
- added REF**387: TestPoint_THTPad_D2.0mm_Drill1.0mm, TestPoint:TestPoint_THTPad_D2.0mm_Drill1.0mm, F.Cu at (218.3, 145.8)
- added REF**388: TestPoint_THTPad_D2.0mm_Drill1.0mm, TestPoint:TestPoint_THTPad_D2.0mm_Drill1.0mm, F.Cu at (220.8, 145.8)
- added REF**389: TestPoint_THTPad_D2.0mm_Drill1.0mm, TestPoint:TestPoint_THTPad_D2.0mm_Drill1.0mm, F.Cu at (223.4, 145.8)
- added REF**4: TestPoint_THTPad_D2.0mm_Drill1.0mm, TestPoint:TestPoint_THTPad_D2.0mm_Drill1.0mm, F.Cu at (159.9, 122.9)
- added REF**402: TestPoint_THTPad_D2.0mm_Drill1.0mm, TestPoint:TestPoint_THTPad_D2.0mm_Drill1.0mm, F.Cu at (154.8, 148.3)
- added REF**403: TestPoint_THTPad_D2.0mm_Drill1.0mm, TestPoint:TestPoint_THTPad_D2.0mm_Drill1.0mm, F.Cu at (157.3, 148.3)
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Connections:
- C19 pad 1: GND -> +3V3
- C19 pad 2: XIN -> GND
- C20 pad 1: GND -> +3V3
- C20 pad 2: Net-(C20-Pad2) -> GND
- C22 pad 1: +5V -> GND
- C22 pad 2: GND -> +3V3
- C23 pad 1: +BATT -> Net-(U4-AC0)
- C23 pad 2: GND -> Net-(U4-AC1)
- C4 pad 1: +5V -> +1V1
- C5 pad 1: +3V3 -> +1V1
- C7 pad 1: +1V1 -> GND
- C7 pad 2: GND -> XIN
- C8 pad 1: +1V1 -> GND
- C8 pad 2: GND -> Net-(C8-Pad2)
- C9 pad 1: +3V3 -> +5V
- Q1 pad 1: +5V -> GDR
- Q1 pad 2: +5V -> RESE
- Q1 pad 3: +BATT -> Net-(D3-A)
- SW3 pad 1: PUSH_1 -> PUSH_3
- SW4 pad 1: PUSH_2 -> PUSH_4
- SW5 pad 1: Net-(J6-Pin_1) -> PUSH_5
- SW5 pad 2: +BATT -> GND
- U5 pad 1: +3V3 -> Net-(U5-VCOM)
- U5 pad 10: PUSH_4 -> +3V3
- U5 pad 11: +3V3 -> MOSI
- U5 pad 12: PUSH_5 -> SCK
- U5 pad 13: PUSH_6 -> CS
- U5 pad 14: NFC_SDA -> D/C
- U5 pad 15: NFC_SCL -> RST
- U5 pad 16: NFC_GPO -> BUSY
- U5 pad 17: CS -> GND
- U5 pad 18: SCK -> unconnected-(U5-TSDA-Pad18)
- U5 pad 19: MOSI -> unconnected-(U5-TSCL-Pad19)
- U5 pad 2: /GPIO0 -> /PREVGL
- U5 pad 20: +3V3 -> Net-(U5-VSH2)
- U5 pad 21: XIN -> Net-(U5-VGL/NC)
- U5 pad 22: XOUT -> RESE
- U5 pad 23: +1V1 -> GDR
- U5 pad 24: SWCLK -> (no net)
- U5 pad 3: /GPIO1 -> Net-(U5-VSL)
- U5 pad 4: /GPIO2 -> /PREVGH
- U5 pad 5: /GPIO3 -> Net-(U5-VSH1)
- U5 pad 6: +1V1 -> Net-(U5-VPP)
- U5 pad 7: PUSH_1 -> Net-(U5-VDD)
- U5 pad 8: PUSH_2 -> GND
- U5 pad 9: PUSH_3 -> +3V3
- Y1 pad 3: Net-(C20-Pad2) -> Net-(C8-Pad2)
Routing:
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- added copper zone on B.Cu, net GND
- added copper zone on F.Cu, net GND
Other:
- board size 7.7 x 0.9 mm -> 108.2 x 99.1 mm

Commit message: update pcb
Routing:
- net +3V3: track 217.2 -> 244.5 mm
- net +5V: track 19.2 -> 20.0 mm
- net GND: track 140.1 -> 140.5 mm, vias 20 -> 31

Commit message: update pcb
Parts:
- moved R11 7.96 mm to (229.4, 90.1), turned to 0 degrees
- moved R9 7.67 mm to (229.4, 89.1), turned to 0 degrees
- moved R14 6.57 mm to (230.6, 86.7), turned to -90 degrees
- moved C22 5.18 mm to (232.1, 86.2), turned to 180 degrees
- moved R13 2.52 mm to (232.4, 82.4)
- moved D4 2.52 mm to (230.1, 82.4)
- moved C23 2.42 mm to (236.0, 89.3), turned to -90 degrees
- moved U4 2.23 mm to (233.3, 88.5), turned to 180 degrees
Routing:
- net +3V3: track 244.5 -> 200.6 mm, vias 10 -> 7
- net NFC_SDA: track 57.8 -> 44.8 mm, vias 4 -> 2
- net NFC_SCL: track 53.2 -> 42.9 mm
- net Net-(U4-AC1): track 9.60 -> 0.00 mm
- net Net-(U4-AC0): track 9.17 -> 0.00 mm
- net NFC_GPO: track 48.6 -> 39.5 mm
- net Net-(D4-A): track 6.61 -> 0.00 mm
- net Net-(D4-K): track 1.61 -> 0.00 mm
- net GND: track 140.5 -> 138.9 mm, vias 31 -> 66
- net PUSH_6: track 95.1 -> 94.5 mm
- net D+: track 76.0 -> 75.4 mm
- net D-: track 77.4 -> 76.7 mm
- net PUSH_5: track 76.3 -> 75.6 mm

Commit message: fix pcb
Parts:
- moved C12 6.33 mm to (249.0, 140.6), turned to 0 degrees
- moved Y1 4.79 mm to (189.7, 97.8)
- moved C7 4.35 mm to (187.3, 99.1), turned to 135 degrees
- moved C8 3.96 mm to (190.8, 94.3)
- moved R6 3.88 mm to (192.1, 95.7)
- moved C16 1.67 mm to (192.0, 100.2), turned to 180 degrees
- moved R11 0.92 mm to (230.2, 90.6)
- moved R9 0.75 mm to (230.2, 89.1)
- moved C5 0.70 mm to (193.8, 96.6)
- moved C23 0.20 mm to (236.0, 89.1)
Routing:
- net +1V1: track 36.1 -> 58.9 mm, vias 4 -> 10
- net GND: track 138.9 -> 116.8 mm, vias 66 -> 52
- net NFC_GPO: track 39.5 -> 55.1 mm, vias 2 -> 4
- net NFC_SCL: track 42.9 -> 53.5 mm, vias 2 -> 4
- net +3V3: track 200.6 -> 210.5 mm, vias 7 -> 4
- net Net-(D4-A): track 0.00 -> 9.80 mm
- net Net-(U4-AC1): track 0.00 -> 9.75 mm
- net Net-(U4-AC0): track 0.00 -> 8.84 mm
- net NFC_SDA: track 44.8 -> 52.1 mm, vias 2 -> 4
- net Net-(D3-A): track 21.3 -> 26.9 mm
- net XOUT: track 10.0 -> 5.92 mm
- net PUSH_6: track 94.5 -> 90.7 mm
- net RST: track 49.1 -> 46.0 mm
- net BUSY: track 48.4 -> 45.3 mm
- net SWD: track 66.1 -> 63.0 mm
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- added copper zone on B.Cu, net +3V3

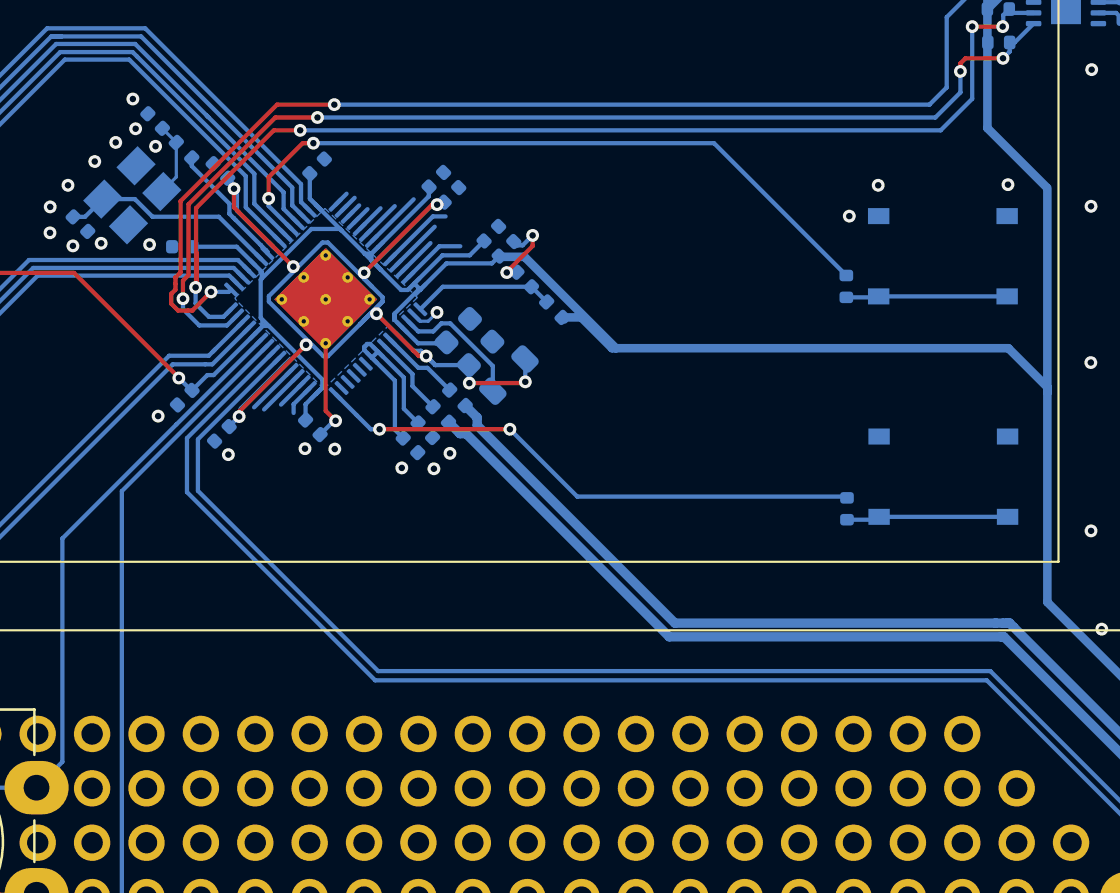
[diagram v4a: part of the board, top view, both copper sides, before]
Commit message: pcb update (add gpio breakouts)
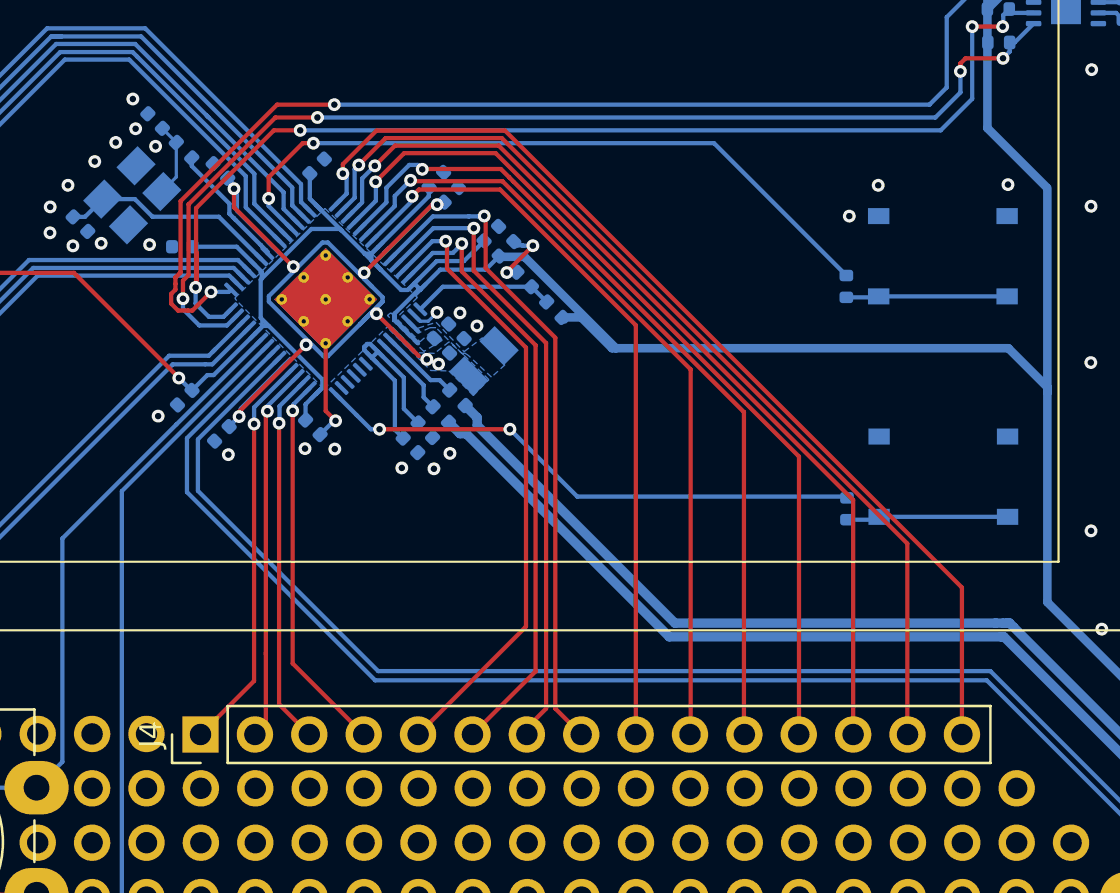
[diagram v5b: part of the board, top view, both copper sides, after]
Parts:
- removed REF**17, REF**18, REF**19, REF**20, REF**21, REF**22, REF**23, REF**24, REF**25, REF**26, REF**27, REF**28, REF**29, REF**30, REF**31: TestPoint_THTPad_D2.0mm_Drill1.0mm, TestPoint:TestPoint_THTPad_D2.0mm_Drill1.0mm
- added J4: Conn_01x14_Pin, Connector_PinHeader_2.54mm:PinHeader_1x15_P2.54mm_Vertical, F.Cu at (192.9, 123.0)
- C1, C2: footprint Capacitor_SMD:C_0603_1608Metric -> Capacitor_SMD:C_0402_1005Metric
- L1: footprint Inductor_SMD:L_0805_2012Metric -> ant:Abracon AOTA-B201610S3R3-101-T
- moved C2 1.17 mm to (204.9, 104.8)
- moved C1 0.79 mm to (204.1, 104.1)
- moved L1 0.46 mm to (206.8, 106.2), turned to 45 degrees
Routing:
- net /GPIO19: track 0.73 -> 47.4 mm, vias 0 -> 1
- net /GPIO20: track 0.86 -> 45.4 mm, vias 0 -> 1
- net /GPIO21: track 0.76 -> 43.4 mm, vias 0 -> 1
- net /GPIO22: track 0.91 -> 41.5 mm, vias 0 -> 1
- net /GPIO23: track 1.37 -> 39.4 mm, vias 0 -> 1
- net /GPIO24: track 1.91 -> 37.2 mm, vias 0 -> 1
- net /GPIO25: track 2.76 -> 35.2 mm, vias 0 -> 1
- net /GPIO26: track 3.42 -> 31.3 mm, vias 0 -> 1
- net /GPIO28: track 1.87 -> 29.3 mm, vias 0 -> 1
- net /GPIO27: track 2.55 -> 29.8 mm, vias 0 -> 1
- net /GPIO29: track 3.04 -> 28.8 mm, vias 0 -> 1
- net /GPIO0: track 1.48 -> 18.1 mm, vias 0 -> 1
- net /GPIO3: track 2.48 -> 18.8 mm, vias 0 -> 1
- net /GPIO1: track 1.50 -> 17.5 mm, vias 0 -> 1
- net /GPIO2: track 2.22 -> 17.7 mm, vias 0 -> 1
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- added copper zone on B.Cu, net +1V1
- added copper zone on B.Cu, net /VREG_LX
